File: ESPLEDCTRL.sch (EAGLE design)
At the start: 11 parts, among them J1 22-27-2031-03, J2 22-27-2041-04, X3 ZX62D-B-5PA8, X4 MINI-USB-32005-201

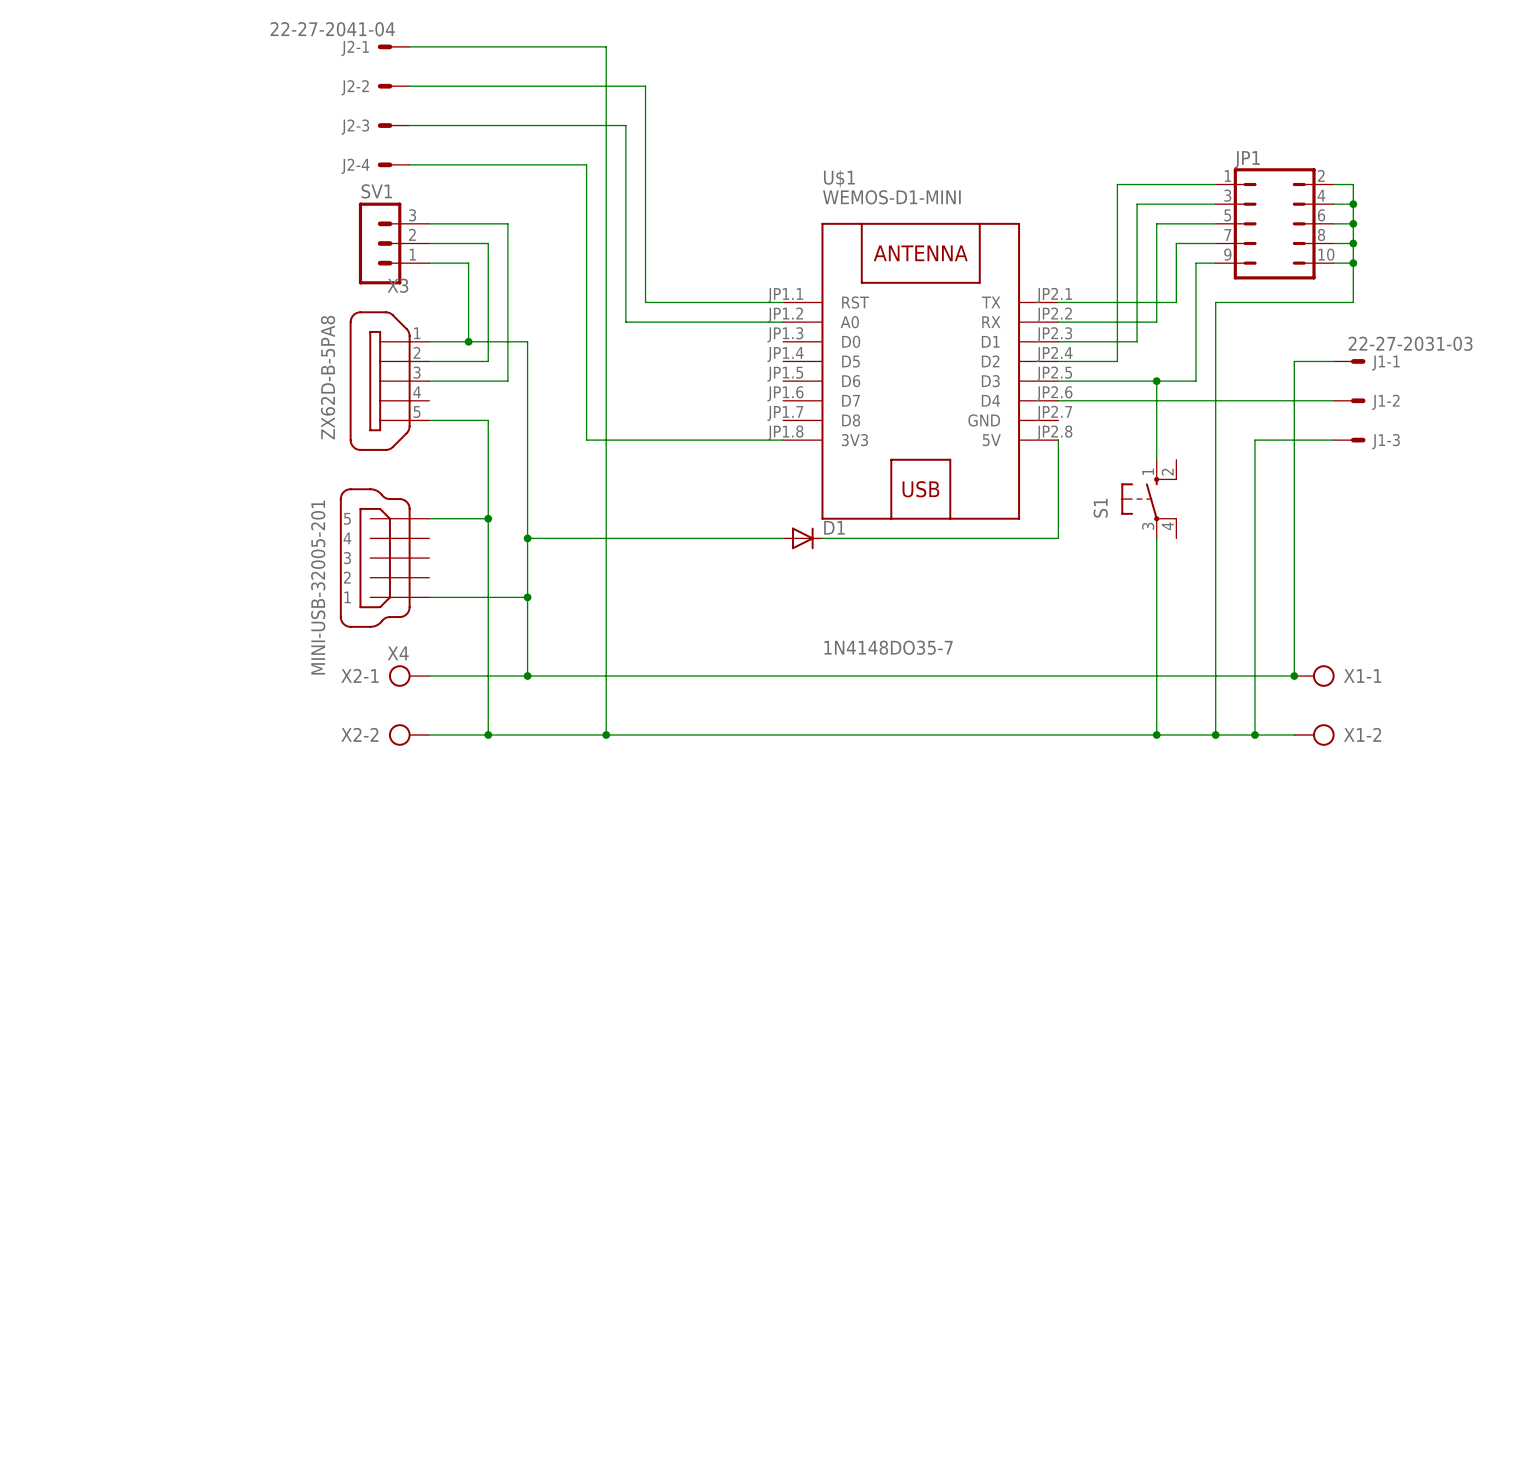
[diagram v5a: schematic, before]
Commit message: Umbau auf Version 2 beginnt
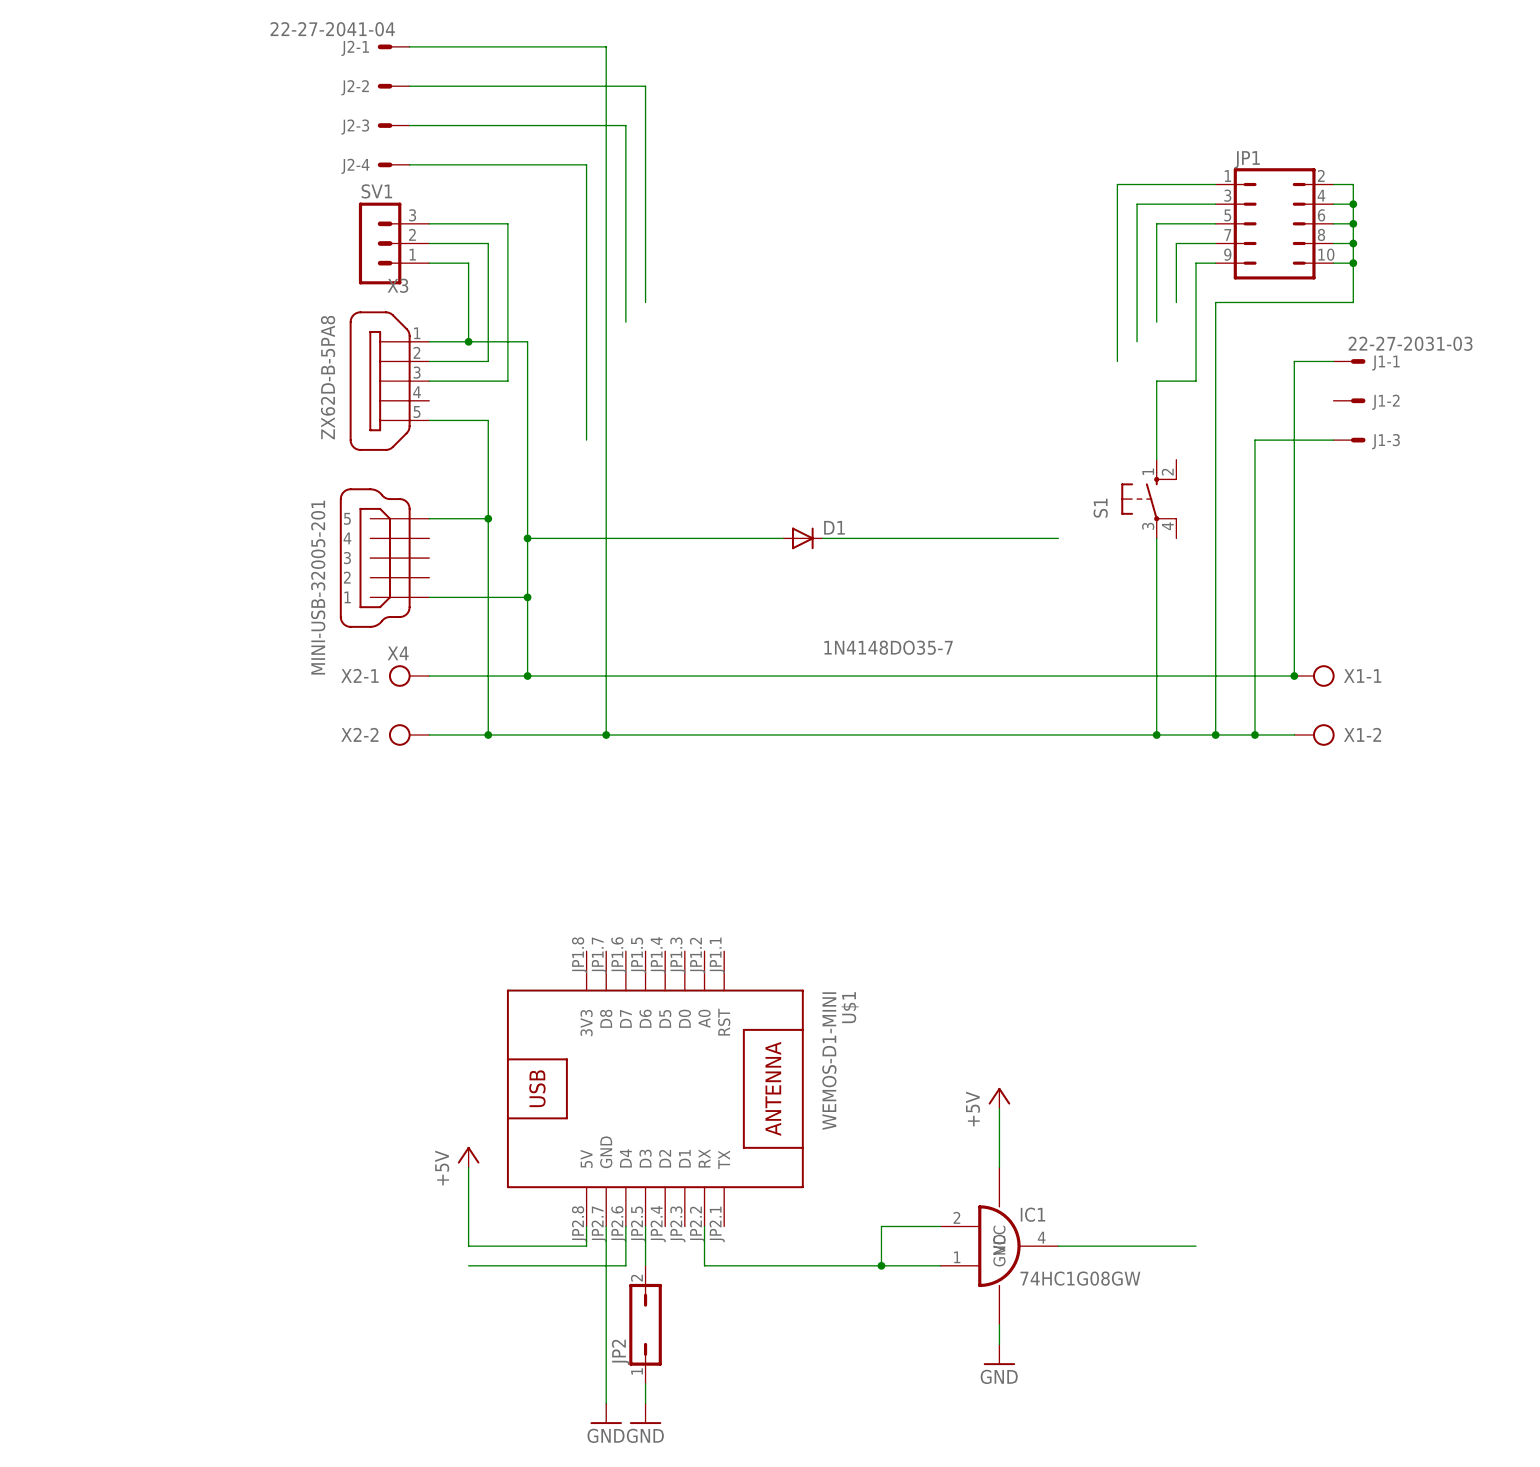
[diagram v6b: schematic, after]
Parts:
- added IC1: 74HC1G08GW, Logik-IC:74HC1G08GW
- added JP2: (no value), jumper:JP1Q
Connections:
- new net +5V: IC1.VCC, U$1.5V
- new net GND: IC1.GND, JP2.1, U$1.GND
- new net N$15: U$1.D4
- new net N$16: IC1.I0, IC1.I1, U$1.RX
- new net N$18: IC1.O
- net N$1: now also JP2.2, U$1.D3; no longer J1-2.S, U$1.D4
- net N$10: no longer U$1.A0
- net N$12: no longer U$1.3V3
- net N$2: no longer U$1.5V
- net N$4: no longer U$1.D3
- net N$5: no longer U$1.D2
- net N$6: no longer U$1.RST
- net N$7: no longer U$1.D1
- net N$8: no longer U$1.RX
- net N$9: no longer U$1.TX
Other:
- moved on the sheet: U$1
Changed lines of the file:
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@@
 <?xml version="1.0" encoding="utf-8"?>
 <!DOCTYPE eagle SYSTEM "eagle.dtd">
-<eagle version="8.7.1">
+<eagle version="8.6.0">
 <drawing>
 <settings>
@@
 <layers>
 <layer number="1" name="Top" color="4" fill="1" visible="no" active="no"/>
+<layer number="2" name="Route2" color="1" fill="3" visible="no" active="no"/>
+<layer number="3" name="Route3" color="4" fill="3" visible="no" active="no"/>
+<layer number="4" name="Route4" color="1" fill="4" visible="no" active="no"/>
+<layer number="5" name="Route5" color="4" fill="4" visible="no" active="no"/>
+<layer number="6" name="Route6" color="1" fill="8" visible="no" active="no"/>
+<layer number="7" name="Route7" color="4" fill="8" visible="no" active="no"/>
+<layer number="8" name="Route8" color="1" fill="2" visible="no" active="no"/>
+<layer number="9" name="Route9" color="4" fill="2" visible="no" active="no"/>
+<layer number="10" name="Route10" color="1" fill="7" visible="no" active="no"/>
+<layer number="11" name="Route11" color="4" fill="7" visible="no" active="no"/>
+<layer number="12" name="Route12" color="1" fill="5" visible="no" active="no"/>
+<layer number="13" name="Route13" color="4" fill="5" visible="no" active="no"/>
+<layer number="14" name="Route14" color="1" fill="6" visible="no" active="no"/>
+<layer number="15" name="Route15" color="4" fill="6" visible="no" active="no"/>
 <layer number="16" name="Bottom" color="1" fill="1" visible="no" active="no"/>
 <layer number="17" name="Pads" color="2" fill="1" visible="no" active="no"/>
@@
 <part name="SV1" library="con-lstb" library_urn="urn:adsk.eagle:library:162" deviceset="MA03-1" device="" package3d_urn="urn:adsk.eagle:package:8339/1"/>
 <part name="X4" library="con-cypressindustries" library_urn="urn:adsk.eagle:library:138" deviceset="MINI-USB-" device="32005-201" package3d_urn="urn:adsk.eagle:package:6443/1"/>
+<part name="JP2" library="jumper" library_urn="urn:adsk.eagle:library:252" deviceset="JP1Q" device="" package3d_urn="urn:adsk.eagle:package:15455/1"/>
+<part name="GND1" library="supply1" library_urn="urn:adsk.eagle:library:371" deviceset="GND" device=""/>
+<part name="GND2" library="supply1" library_urn="urn:adsk.eagle:library:371" deviceset="GND" device=""/>
+<part name="IC1" library="Logik-IC" deviceset="74HC1G08" device="GW"/>
+<part name="P+1" library="supply1" library_urn="urn:adsk.eagle:library:371" deviceset="+5V" device=""/>
+<part name="GND3" library="supply1" library_urn="urn:adsk.eagle:library:371" deviceset="GND" device=""/>
+<part name="P+2" library="supply1" library_urn="urn:adsk.eagle:library:371" deviceset="+5V" device=""/>
 </parts>
 <sheets>
@@
 <attribute name="VALUE" x="-1.27" y="50.8" size="1.778" layer="96" font="vector" rot="MR90"/>
 </instance>
-<instance part="U$1" gate="G$1" x="76.2" y="58.42" smashed="yes">
-<attribute name="NAME" x="63.5" y="83.82" size="1.778" layer="95"/>
-<attribute name="VALUE" x="63.5" y="81.28" size="1.778" layer="96"/>
+<instance part="U$1" gate="G$1" x="40.64" y="-33.02" smashed="yes" rot="R270">
+<attribute name="NAME" x="66.04" y="-20.32" size="1.778" layer="95" rot="R270"/>
+<attribute name="VALUE" x="63.5" y="-20.32" size="1.778" layer="96" rot="R270"/>
 </instance>
 <instance part="X1" gate="-1" x="129.54" y="20.32" smashed="yes" rot="R180">
@@
 <instance part="SV1" gate="G$1" x="5.08" y="76.2"/>
 <instance part="X4" gate="G$1" x="7.62" y="35.56" rot="R180"/>
+<instance part="JP2" gate="A" x="40.64" y="-63.5"/>
+<instance part="GND1" gate="1" x="40.64" y="-76.2"/>
+<instance part="GND2" gate="1" x="35.56" y="-76.2"/>
+<instance part="IC1" gate="G$1" x="86.36" y="-53.34"/>
+<instance part="P+1" gate="1" x="86.36" y="-33.02"/>
+<instance part="GND3" gate="1" x="86.36" y="-68.58"/>
+<instance part="P+2" gate="1" x="17.78" y="-40.64"/>
 </instances>
 <busses>
 </busses>
 <nets>
-<net name="N$1" class="0">
-<segment>
-<pinref part="J1" gate="-2" pin="S"/>
-<pinref part="U$1" gate="G$1" pin="D4"/>
-<wire x1="129.54" y1="55.88" x2="93.98" y2="55.88" width="0.1524" layer="91"/>
-</segment>
-</net>
 <net name="N$2" class="0">
 <segment>
 <pinref part="D1" gate="G$1" pin="C"/>
-<pinref part="U$1" gate="G$1" pin="5V"/>
 <wire x1="63.5" y1="38.1" x2="93.98" y2="38.1" width="0.1524" layer="91"/>
-<wire x1="93.98" y1="38.1" x2="93.98" y2="50.8" width="0.1524" layer="91"/>
 </segment>
 </net>
 <net name="N$4" class="0">
 <segment>
-<pinref part="U$1" gate="G$1" pin="D3"/>
-<wire x1="93.98" y1="58.42" x2="106.68" y2="58.42" width="0.1524" layer="91"/>
 <pinref part="S1" gate="1" pin="S"/>
 <wire x1="106.68" y1="58.42" x2="106.68" y2="48.26" width="0.1524" layer="91"/>
@@
 <wire x1="111.76" y1="73.66" x2="111.76" y2="58.42" width="0.1524" layer="91"/>
 <wire x1="111.76" y1="58.42" x2="106.68" y2="58.42" width="0.1524" layer="91"/>
-<junction x="106.68" y="58.42"/>
 </segment>
 </net>
@@
 <wire x1="114.3" y1="83.82" x2="101.6" y2="83.82" width="0.1524" layer="91"/>
 <wire x1="101.6" y1="83.82" x2="101.6" y2="60.96" width="0.1524" layer="91"/>
-<pinref part="U$1" gate="G$1" pin="D2"/>
-<wire x1="101.6" y1="60.96" x2="93.98" y2="60.96" width="0.1524" layer="91"/>
 </segment>
 </net>
@@
 <wire x1="114.3" y1="81.28" x2="104.14" y2="81.28" width="0.1524" layer="91"/>
 <wire x1="104.14" y1="81.28" x2="104.14" y2="63.5" width="0.1524" layer="91"/>
-<pinref part="U$1" gate="G$1" pin="D1"/>
-<wire x1="104.14" y1="63.5" x2="93.98" y2="63.5" width="0.1524" layer="91"/>
 </segment>
 </net>
@@
 <wire x1="114.3" y1="78.74" x2="106.68" y2="78.74" width="0.1524" layer="91"/>
 <wire x1="106.68" y1="78.74" x2="106.68" y2="66.04" width="0.1524" layer="91"/>
-<pinref part="U$1" gate="G$1" pin="RX"/>
-<wire x1="106.68" y1="66.04" x2="93.98" y2="66.04" width="0.1524" layer="91"/>
 </segment>
 </net>
@@
 <wire x1="114.3" y1="76.2" x2="109.22" y2="76.2" width="0.1524" layer="91"/>
 <wire x1="109.22" y1="76.2" x2="109.22" y2="68.58" width="0.1524" layer="91"/>
-<pinref part="U$1" gate="G$1" pin="TX"/>
-<wire x1="109.22" y1="68.58" x2="93.98" y2="68.58" width="0.1524" layer="91"/>
 </segment>
 </net>
@@
 <net name="N$6" class="0">
 <segment>
-<pinref part="U$1" gate="G$1" pin="RST"/>
-<wire x1="58.42" y1="68.58" x2="40.64" y2="68.58" width="0.1524" layer="91"/>
 <pinref part="J2" gate="-2" pin="S"/>
 <wire x1="40.64" y1="68.58" x2="40.64" y2="96.52" width="0.1524" layer="91"/>
@@
 <net name="N$10" class="0">
 <segment>
-<pinref part="U$1" gate="G$1" pin="A0"/>
-<wire x1="58.42" y1="66.04" x2="38.1" y2="66.04" width="0.1524" layer="91"/>
 <wire x1="38.1" y1="66.04" x2="38.1" y2="91.44" width="0.1524" layer="91"/>
 <pinref part="J2" gate="-3" pin="S"/>
@@
 <wire x1="10.16" y1="86.36" x2="33.02" y2="86.36" width="0.1524" layer="91"/>
 <wire x1="33.02" y1="86.36" x2="33.02" y2="50.8" width="0.1524" layer="91"/>
-<pinref part="U$1" gate="G$1" pin="3V3"/>
-<wire x1="33.02" y1="50.8" x2="58.42" y2="50.8" width="0.1524" layer="91"/>
 </segment>
 </net>
@@
 </segment>
 </net>
+<net name="N$1" class="0">
+<segment>
+<pinref part="U$1" gate="G$1" pin="D3"/>
+<wire x1="40.64" y1="-50.8" x2="40.64" y2="-55.88" width="0.1524" layer="91"/>
+<pinref part="JP2" gate="A" pin="2"/>
+</segment>
+</net>
+<net name="GND" class="0">
+<segment>
+<pinref part="JP2" gate="A" pin="1"/>
+<pinref part="GND1" gate="1" pin="GND"/>
+<wire x1="40.64" y1="-71.12" x2="40.64" y2="-73.66" width="0.1524" layer="91"/>
+</segment>
+<segment>
+<pinref part="U$1" gate="G$1" pin="GND"/>
+<pinref part="GND2" gate="1" pin="GND"/>
+<wire x1="35.56" y1="-50.8" x2="35.56" y2="-73.66" width="0.1524" layer="91"/>
+</segment>
+<segment>
+<pinref part="IC1" gate="G$1" pin="GND"/>
+<pinref part="GND3" gate="1" pin="GND"/>
+<wire x1="86.36" y1="-66.04" x2="86.36" y2="-63.5" width="0.1524" layer="91"/>
+</segment>
+</net>
+<net name="N$15" class="0">
+<segment>
+<pinref part="U$1" gate="G$1" pin="D4"/>
+<wire x1="38.1" y1="-50.8" x2="38.1" y2="-55.88" width="0.1524" layer="91"/>
+<wire x1="38.1" y1="-55.88" x2="17.78" y2="-55.88" width="0.1524" layer="91"/>
+</segment>
+</net>
+<net name="N$16" class="0">
+<segment>
+<pinref part="U$1" gate="G$1" pin="RX"/>
+<wire x1="48.26" y1="-50.8" x2="48.26" y2="-55.88" width="0.1524" layer="91"/>
+<wire x1="48.26" y1="-55.88" x2="71.12" y2="-55.88" width="0.1524" layer="91"/>
+<pinref part="IC1" gate="G$1" pin="I0"/>
+<wire x1="78.74" y1="-50.8" x2="71.12" y2="-50.8" width="0.1524" layer="91"/>
+<wire x1="71.12" y1="-50.8" x2="71.12" y2="-55.88" width="0.1524" layer="91"/>
+<pinref part="IC1" gate="G$1" pin="I1"/>
+<wire x1="78.74" y1="-55.88" x2="71.12" y2="-55.88" width="0.1524" layer="91"/>
+<junction x="71.12" y="-55.88"/>
+</segment>
+</net>
+<net name="N$18" class="0">
+<segment>
+<pinref part="IC1" gate="G$1" pin="O"/>
+<wire x1="93.98" y1="-53.34" x2="111.76" y2="-53.34" width="0.1524" layer="91"/>
+</segment>
+</net>
+<net name="+5V" class="0">
+<segment>
+<pinref part="IC1" gate="G$1" pin="VCC"/>
+<pinref part="P+1" gate="1" pin="+5V"/>
+<wire x1="86.36" y1="-35.56" x2="86.36" y2="-43.18" width="0.1524" layer="91"/>
+</segment>
+<segment>
+<pinref part="U$1" gate="G$1" pin="5V"/>
+<wire x1="33.02" y1="-50.8" x2="33.02" y2="-53.34" width="0.1524" layer="91"/>
+<pinref part="P+2" gate="1" pin="+5V"/>
+<wire x1="33.02" y1="-53.34" x2="17.78" y2="-53.34" width="0.1524" layer="91"/>
+<wire x1="17.78" y1="-53.34" x2="17.78" y2="-43.18" width="0.1524" layer="91"/>
+</segment>
+</net>
